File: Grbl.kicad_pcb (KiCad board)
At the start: 2 copper layers, 68.5 x 56.6 mm, 20 parts, among them P1 CTL, P2 MISC, P3 STEP, P4 SPIN, P5 LIMIT

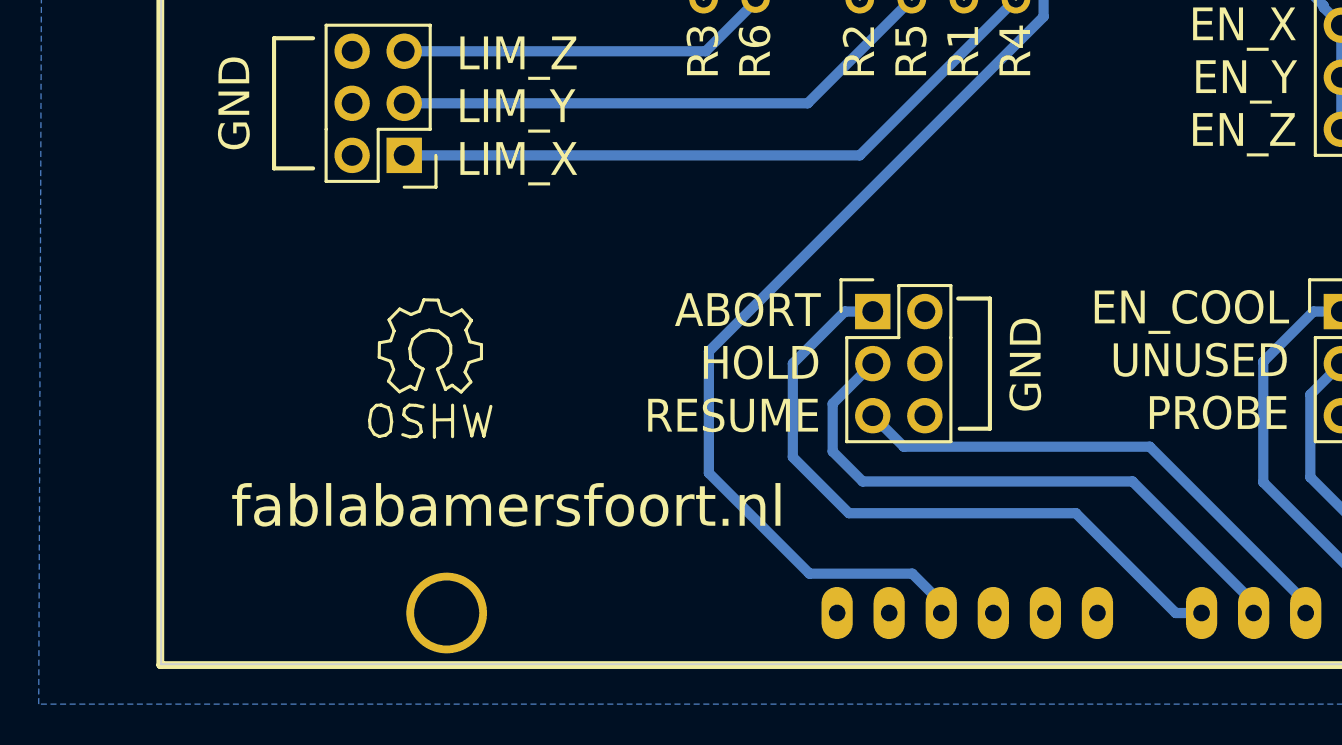
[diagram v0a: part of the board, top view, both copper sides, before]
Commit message: Add more ground pins
This helps connecting the shield wire of cables.
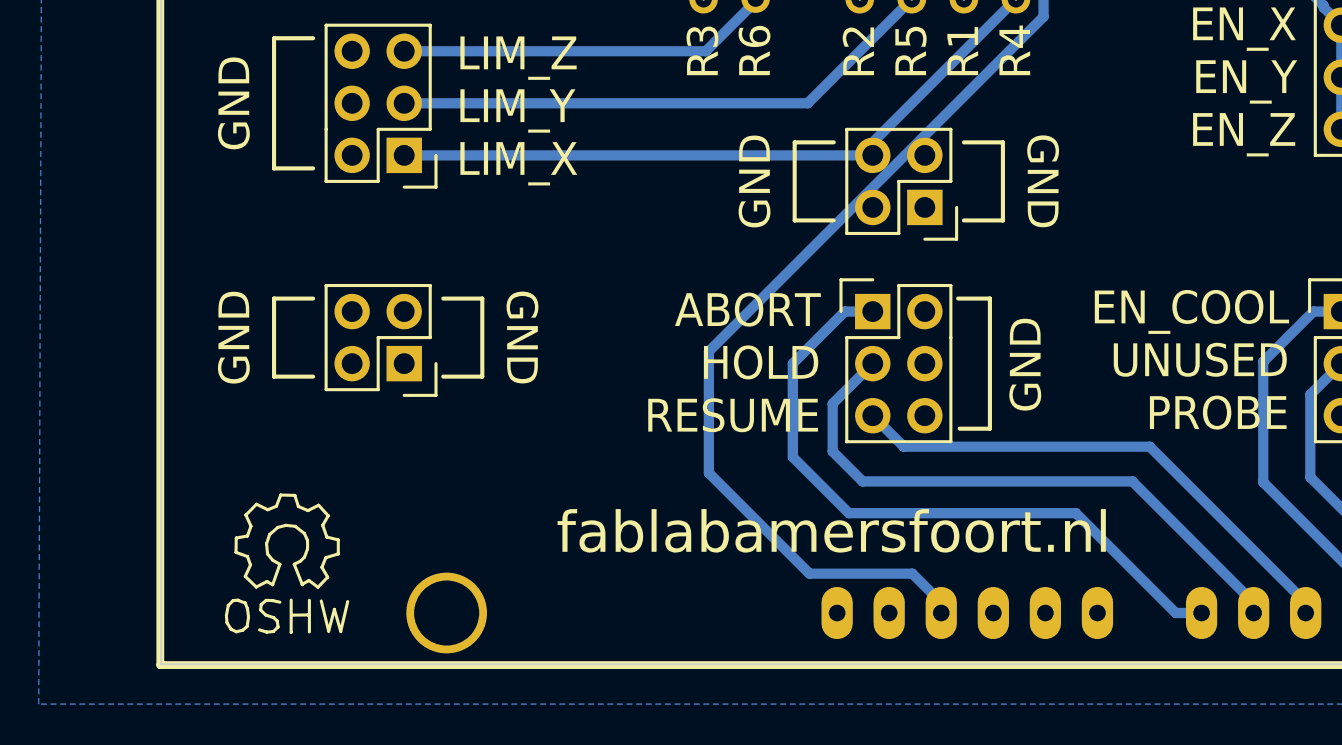
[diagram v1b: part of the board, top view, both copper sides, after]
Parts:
- added P6: GND, Pin_Headers:Pin_Header_Straight_2x02, F.Cu at (160.0, 109.2)
- added P7: GND, Pin_Headers:Pin_Header_Straight_2x02, F.Cu at (185.4, 101.6)
- C1, C3, C5: value 22n -> 10n
- moved REF** 11.8 mm to (154.3, 118.1)
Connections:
- SHIELD1 pad 0: (no net) -> Net-(SHIELD1-Pad0)
- SHIELD1 pad 1: (no net) -> Net-(SHIELD1-Pad1)
- SHIELD1 pad 3V3: (no net) -> Net-(SHIELD1-Pad3V3)
- SHIELD1 pad AREF: (no net) -> Net-(SHIELD1-PadAREF)
- SHIELD1 pad RST: (no net) -> Net-(SHIELD1-PadRST)
- SHIELD1 pad V_IN: (no net) -> Net-(SHIELD1-PadV_IN)
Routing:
- net GND: track 0.18 -> 11.0 mm
- net /LIM_X: track 33.0 -> 22.2 mm
